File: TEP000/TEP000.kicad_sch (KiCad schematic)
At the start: 12 parts

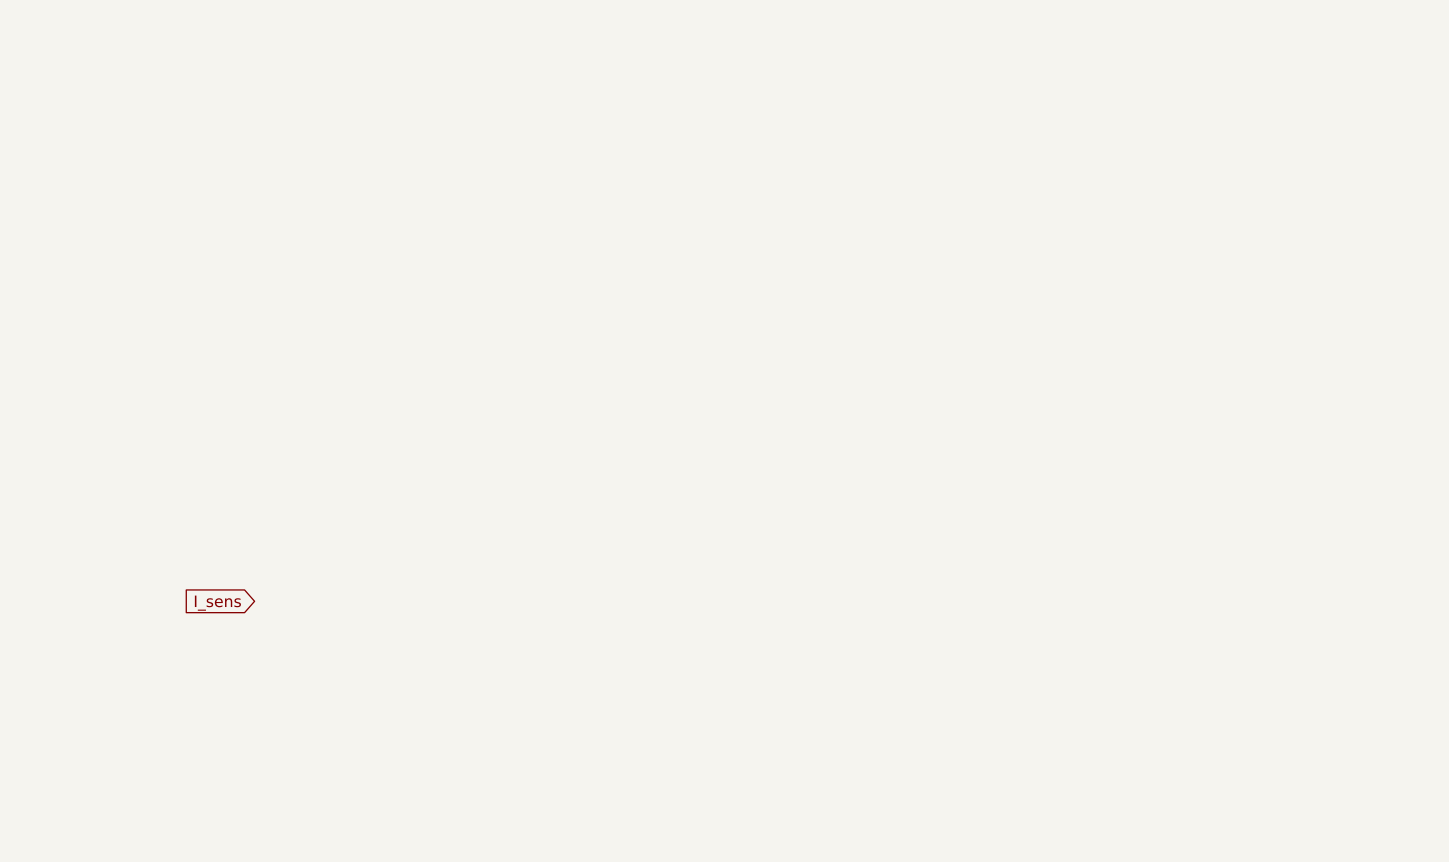
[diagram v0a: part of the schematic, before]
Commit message: added transimpedance amplifier
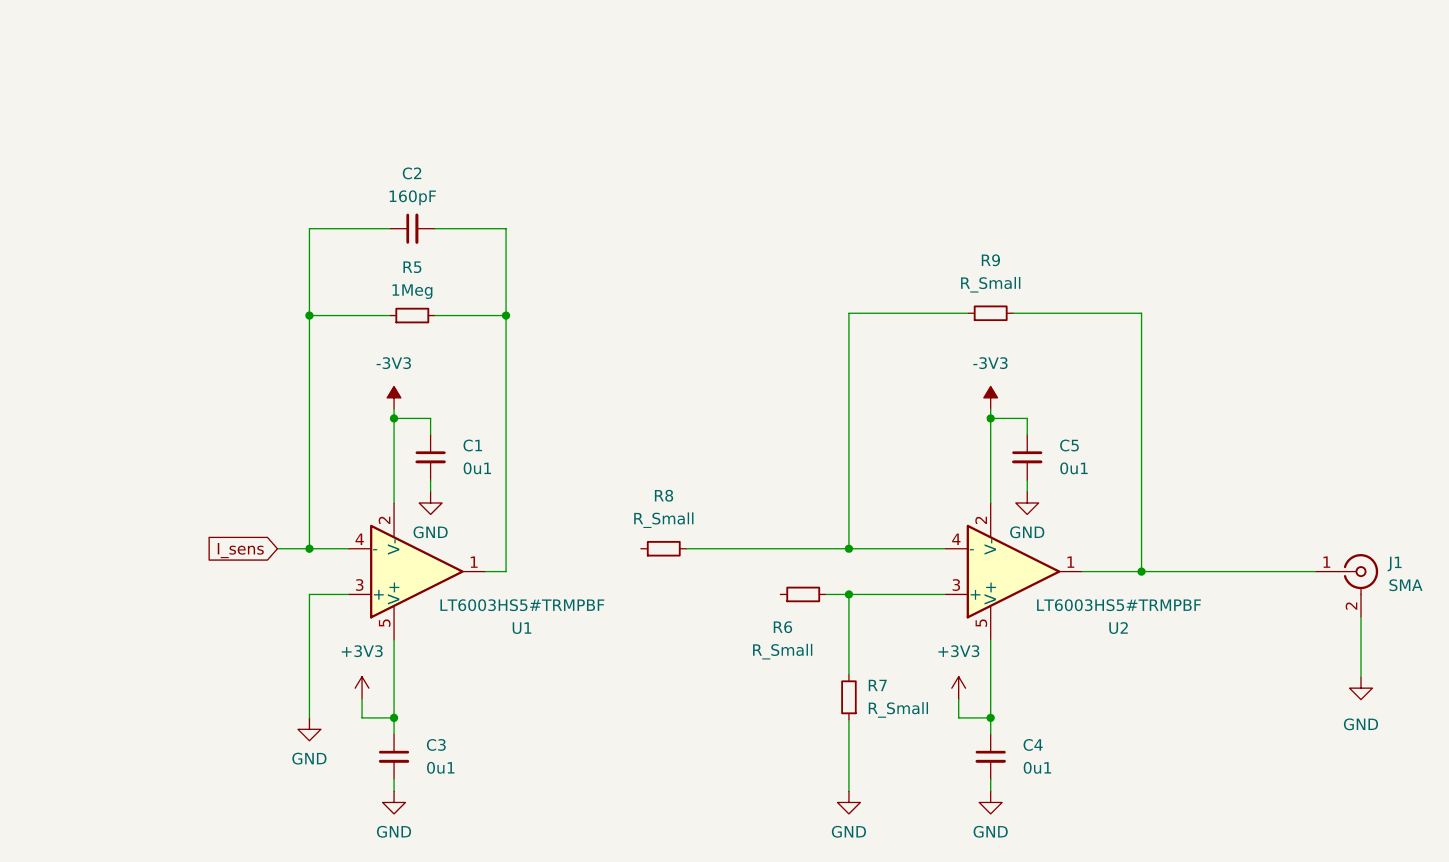
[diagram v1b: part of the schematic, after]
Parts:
- added C1, C3, C4, C5: 0u1, symbol Device:C_Small
- added C2: 160pF, symbol Device:C_Small
- added J1: SMA, symbol Connector:Conn_Coaxial
- added R5: 1Meg, symbol Device:R_Small
- added R6, R7, R8, R9: R_Small, symbol Device:R_Small
- added U1, U2: LT6003HS5#TRMPBF, Package_TO_SOT_SMD:SOT-23-5, symbol Amplifier_Operational:LT6015xS5
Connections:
- net GND: now also C1.2, C3.2, C4.2, C5.2, J1.2 (Ext), R7.1, U1.3 (+)
- net I_sens: now also C2.1, R5.1, U1.4 (-)
- new net: C2.2, R5.2, U1.1
- new net: J1.1 (In), R9.2, U2.1
- new net: R6.2, R7.2, U2.3 (+)
- new net: R8.2, R9.1, U2.4 (-)
- new net +3V3: C3.1, C4.1, U1.5 (V+), U2.5 (V+)
- new net -3V3: C1.1, C5.1, U1.2 (V-), U2.2 (V-)

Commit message: First rev of TEP000 Prototype
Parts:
- removed R9: R_Small, symbol Device:R_Small
- removed U2: LT6003HS5#TRMPBF, Package_TO_SOT_SMD:SOT-23-5, symbol Amplifier_Operational:LT6015xS5
- added C10, C11, C6, C7, C8, C9: 10uF, Capacitor_SMD:C_0805_2012Metric, symbol Device:C_Small
- added FB1, FB2: MMZ2012Y600BT000, Capacitor_SMD:C_0805_2012Metric_Pad1.18x1.45mm_HandSolder, symbol Device:FerriteBead_Small
- added J2: Molex, MyFootPrints:Screwterminal_3mm81_3pos, symbol Connector:Screw_Terminal_01x03
- added U2: MAX889TESA+, Package_SO:SO-8_3.9x4.9mm_P1.27mm, symbol MySymbols:MAX889TESA+
- added U3: XC6209F332MR-G, Package_TO_SOT_SMD:SOT-89-5, symbol MySymbols:XC6209F332MR-G
- added U4: XC6902N331MR-G, Package_TO_SOT_SMD:SOT-23_Handsoldering, symbol MySymbols:XC6902N331MR-G
- C1, C2, C3: footprint (none) -> Capacitor_SMD:C_0805_2012Metric
- C4: value 0u1 -> 1uF; footprint (none) -> Capacitor_SMD:C_0805_2012Metric
- C5: value 0u1 -> 10uF; footprint (none) -> Capacitor_SMD:C_0805_2012Metric
- D1, D2, D3, D4: footprint (none) -> Diode_SMD:D_0603_1608Metric
- D5, D6, D7, D8: footprint (none) -> MyFootPrints:TEMD5510FX01
- J1: footprint (none) -> Connector_Coaxial:SMA_Amphenol_901-143_Horizontal
- R1, R2, R3, R4, R5: footprint (none) -> Resistor_SMD:R_0805_2012Metric
- R6: value R_Small -> 100R; footprint (none) -> Resistor_SMD:R_0805_2012Metric
- R7: value R_Small -> 100k; footprint (none) -> Resistor_SMD:R_0805_2012Metric
- R8: value R_Small -> 91k; footprint (none) -> Resistor_SMD:R_0805_2012Metric
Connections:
- net +3V3: now also C9.1, U3.5 (VOUT); no longer C4.1
- net +5V: now also C5.1, D5.1 (K), D6.1 (K), D7.1 (K), D8.1 (K), R7.2, C11.2, C6.1, FB1.1, U2.1 (IN), U2.6 (/SHDN), U3.3 (CE), U3.4 (VIN); no longer D5.2 (A), D6.2 (A), D7.2 (A), D8.2 (A)
- net -3V3: now also C10.1, U4.1 (-VOUT); no longer C5.1
- net GND: now also C10.2, C11.1, C6.2, C7.2, C8.2, C9.2, J2.3 (Pin_3), U2.3 (GND), U2.8 (AGND), U3.2 (VSS), U4.2 (GND); no longer C4.2, R7.1
- net at C2.2, R5.2, U1.1: now also R6.1
- net at J1.1 (In): now also R6.2
- net at R8.2: now also C7.1, FB2.1, U2.5 (OUT)
- net at R8.1: now also R7.1, U2.7 (FB)
- removed net I_sens: C2.1, D5.1 (K), D6.1 (K), D7.1 (K), D8.1 (K), R5.1, U1.4 (-)
- new net: C8.1, FB2.2, U4.3 (-IN)
- new net: C4.1, U2.2 (CAP+)
- new net: C4.2, U2.4 (CAP-)
- new net: C2.1, D5.2 (A), D6.2 (A), D7.2 (A), D8.2 (A), R5.1, U1.4 (-)
- new net: FB1.2, J2.1 (Pin_1)
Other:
- moved on the sheet: C1, C2, C3, D1, D2, D3, D4, D5, D6, D7, D8, J1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

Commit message: Started work on rev AB
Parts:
- removed C10, C11, C6, C7, C8, C9: 10uF, Capacitor_SMD:C_0805_2012Metric, symbol Device:C_Small
- removed D5, D6, D7: TEMD5510FX01, MyFootPrints:TEMD5510FX01, symbol Device:D_Photo
- removed FB1, FB2: MMZ2012Y600BT000, Capacitor_SMD:C_0805_2012Metric_Pad1.18x1.45mm_HandSolder, symbol Device:FerriteBead_Small
- removed J1: SMA, Connector_Coaxial:SMA_Amphenol_901-143_Horizontal, symbol Connector:Conn_Coaxial
- removed J2: Molex, MyFootPrints:Screwterminal_3mm81_3pos, symbol Connector:Screw_Terminal_01x03
- removed U2: MAX889TESA+, Package_SO:SO-8_3.9x4.9mm_P1.27mm, symbol MySymbols:MAX889TESA+
- removed U3: XC6209F332MR-G, Package_TO_SOT_SMD:SOT-89-5, symbol MySymbols:XC6209F332MR-G
- removed U4: XC6902N331MR-G, Package_TO_SOT_SMD:SOT-23_Handsoldering, symbol MySymbols:XC6902N331MR-G
- added Q1: 2N7002k-7, symbol Device:Q_NMOS_GSD
- added Q2: BC849C,125, Package_TO_SOT_SMD:SOT-23, symbol Transistor_BJT:BC849
- added R10, R11, R9: 100R, Resistor_SMD:R_0805_2012Metric, symbol Device:R_Small
- added TP1: OHR_O, symbol Connector:TestPoint_Small
- added TP2: GND, symbol Connector:TestPoint_Small
- added U2: MCP6006T-E/LT, symbol Amplifier_Operational:LT6015xS5
- C1: value 0u1 -> F
- C4: value 1uF -> 0u1; footprint Capacitor_SMD:C_0805_2012Metric -> (none)
- C5: value 10uF -> 0u1
- R6: value 100R -> R
- R8: value 91k -> 100k
- U1: value LT6003HS5#TRMPBF -> MCP6006T-E/LT; footprint Package_TO_SOT_SMD:SOT-23-5 -> (none); Farnell (none) -> 3807531
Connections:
- net +3V3 is gone; now on net +3.3VA: C3.1, U1.5 (V+)
- net GND: now also C4.2, R8.2, U1.2 (V-), Q1.2 (S), R10.2, TP2.1, U2.2 (V-); no longer C1.2, D1.1 (K), D2.1 (K), D3.1 (K), D4.1 (K), U1.3 (+)
- net Vref: now reaches C4.1
- net Vref: now also R7.2, R8.1, U1.3 (+), U2.3 (+)
- net at C2.2, R5.2, R6.1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: now also R11.2
- net at C2.1, D8.2 (A), R5.1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: now also Q2.3 (C)
- net at R6.2: now also C1.2, U2.4 (-)
- net +3.3VA: now reaches R7.1
- net +3.3VA: now also C5.1, D8.1 (K), R1.1, R2.1, R3.1, R4.1, U2.5 (V+); no longer R8.1
- removed net +5V: C5.1, D8.1 (K), R1.1, R2.1, R3.1, R4.1, R7.2
- net -3V3: no longer names the net of C1.1
- net -3V3: now also R9.1, U2.1; no longer U1.2 (V-)
- new net: Q2.1 (B), R9.2
- new net: Q2.2 (E), R10.1
- new net: D1.1 (K), D2.1 (K), D3.1 (K), D4.1 (K), Q1.3 (D)
- new net LED_EN: Q1.1 (G)
- new net OHR_ADC: R11.1, TP1.1
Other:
- moved on the sheet: C2, C3, D1, D2, D3, D4, D8, R1, R2, R3, R4, R5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

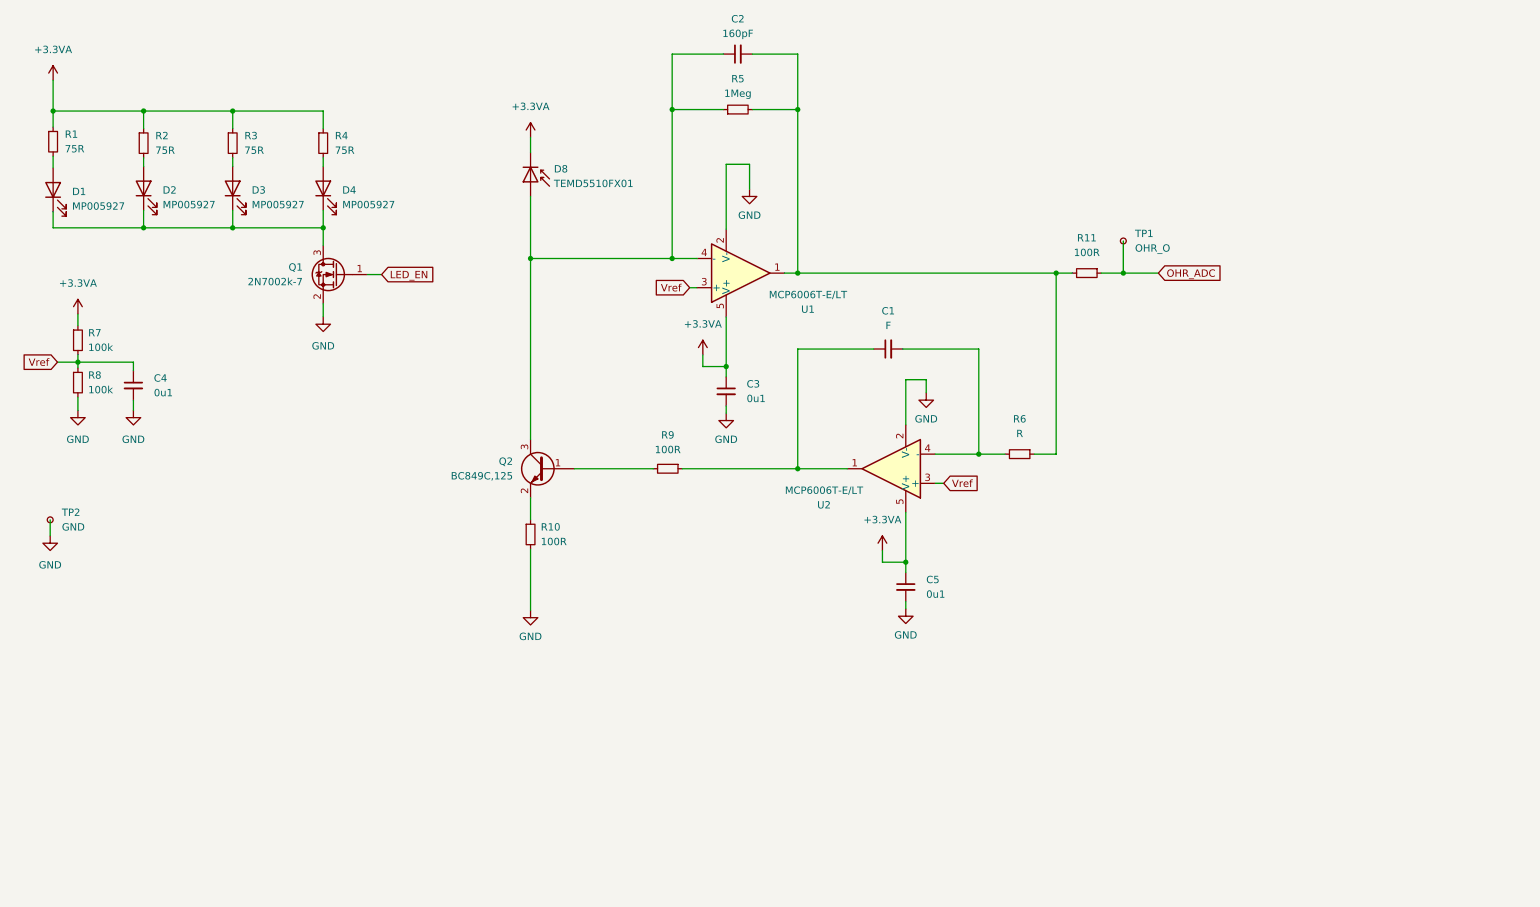
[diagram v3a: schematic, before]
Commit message: TEP000AB
Added buck-boost converters, MCU and integrator bleed circuit.
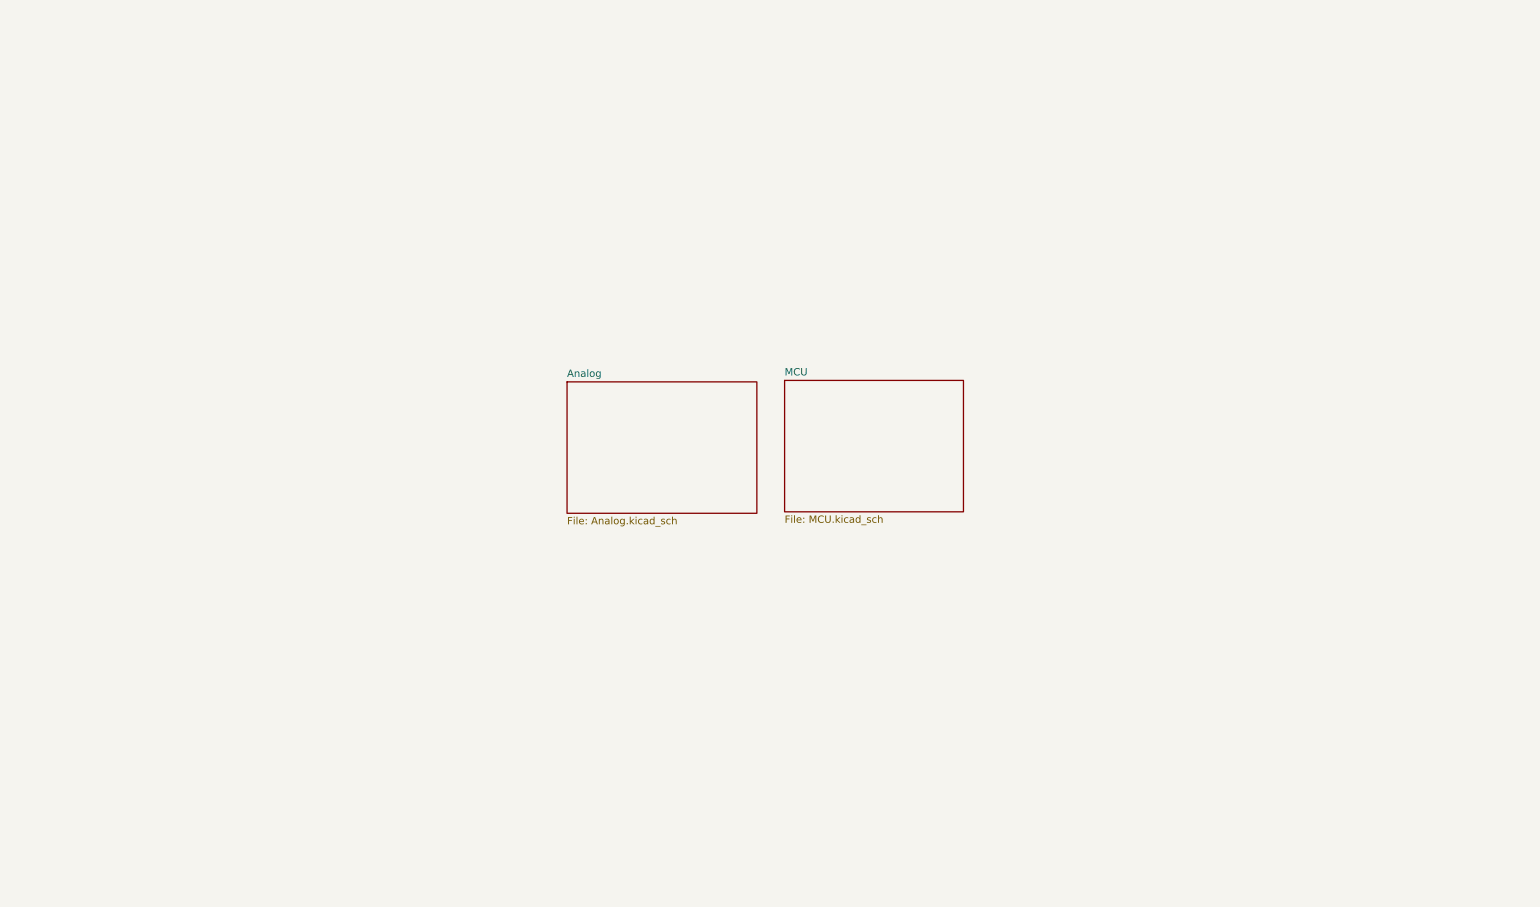
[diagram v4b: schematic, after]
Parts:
- removed C1: F, Capacitor_SMD:C_0805_2012Metric, symbol Device:C_Small
- removed C2: 160pF, Capacitor_SMD:C_0805_2012Metric, symbol Device:C_Small
- removed C3, C5: 0u1, Capacitor_SMD:C_0805_2012Metric, symbol Device:C_Small
- removed C4: 0u1, symbol Device:C_Small
- removed D1, D2, D3, D4: MP005927, Diode_SMD:D_0603_1608Metric, symbol Device:LED
- removed D8: TEMD5510FX01, MyFootPrints:TEMD5510FX01, symbol Device:D_Photo
- removed Q1: 2N7002k-7, symbol Device:Q_NMOS_GSD
- removed Q2: BC849C,125, Package_TO_SOT_SMD:SOT-23, symbol Transistor_BJT:BC849
- removed R1, R2, R3, R4: 75R, Resistor_SMD:R_0805_2012Metric, symbol Device:R_Small
- removed R10, R11, R9: 100R, Resistor_SMD:R_0805_2012Metric, symbol Device:R_Small
- removed R5: 1Meg, Resistor_SMD:R_0805_2012Metric, symbol Device:R_Small
- removed R6: R, Resistor_SMD:R_0805_2012Metric, symbol Device:R_Small
- removed R7, R8: 100k, Resistor_SMD:R_0805_2012Metric, symbol Device:R_Small
- removed TP1: OHR_O, symbol Connector:TestPoint_Small
- removed TP2: GND, symbol Connector:TestPoint_Small
- removed U1, U2: MCP6006T-E/LT, symbol Amplifier_Operational:LT6015xS5
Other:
- added sheet Analog (Analog.kicad_sch)
- added sheet MCU (MCU.kicad_sch)
